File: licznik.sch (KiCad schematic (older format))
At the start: 23 parts, among them J1 Display, J2 Micro_SD_Card_Det, J3 Serial CS1, J4 Serial CS2, SW1 Wheel, SW2 Crank, SW3 Backlight, SW4 Right, SW5 Select, SW6 Left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

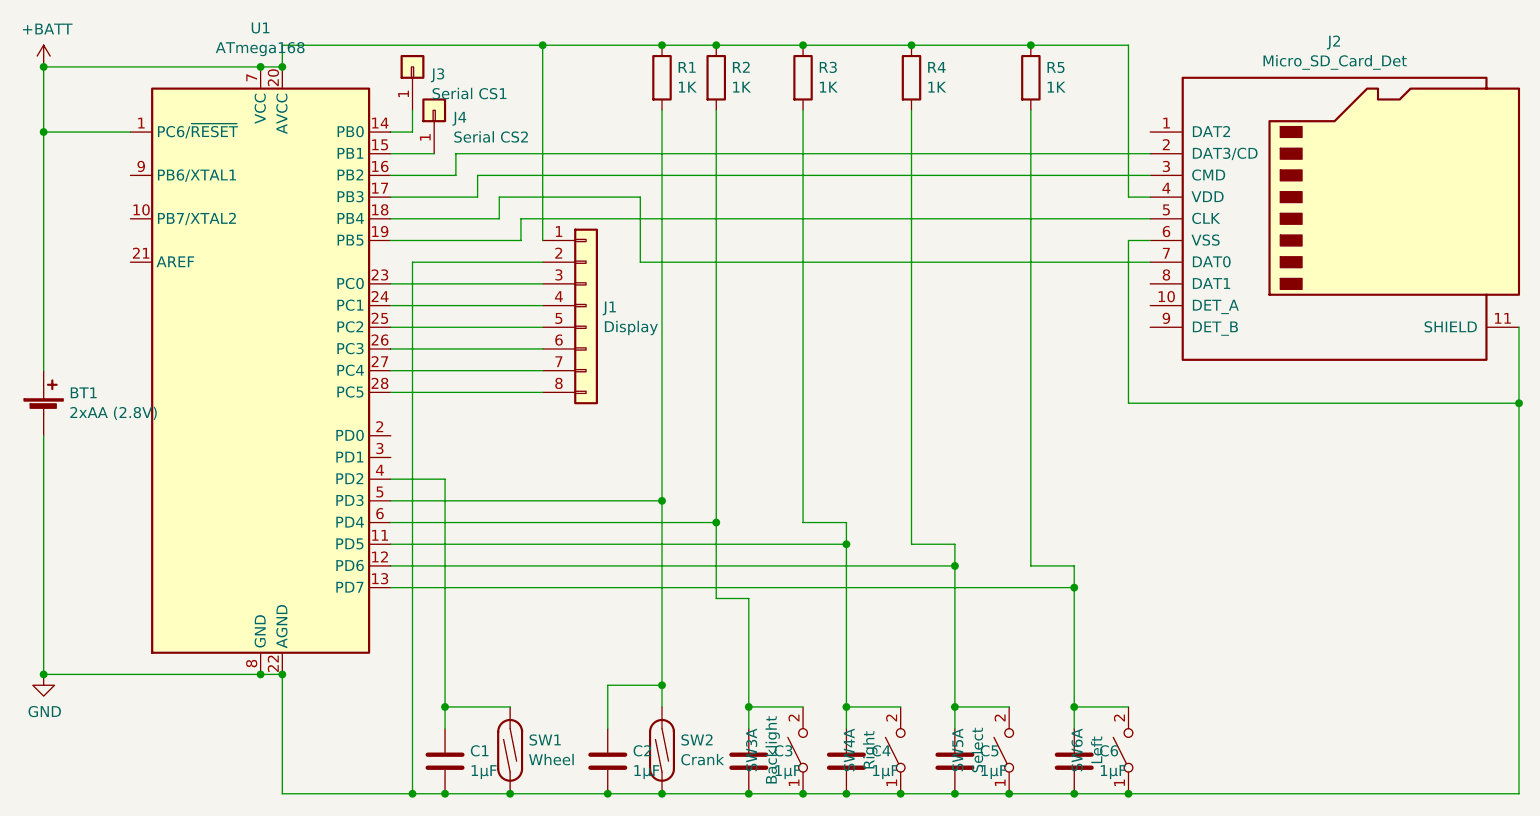
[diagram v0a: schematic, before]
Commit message: Add crank pull up resistor
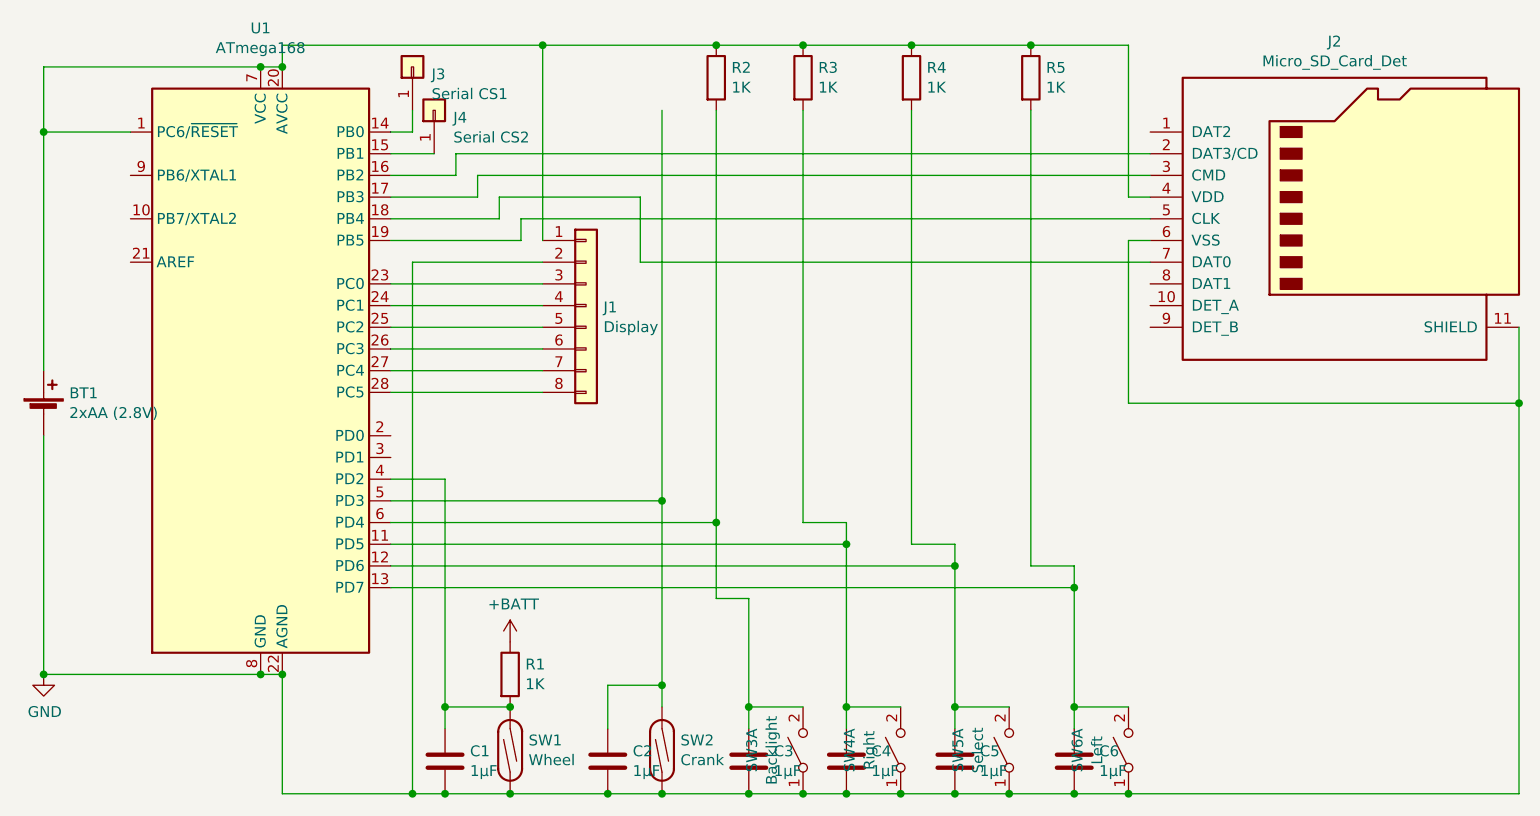
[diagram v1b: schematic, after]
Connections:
- net +BATT: no longer BT1.1 (+), J1.1 (Pin_1), J2.4 (VDD), R2.1, R3.1, R4.1, R5.1, U1.1 (PC6/~RESET), U1.20 (AVCC), U1.7 (VCC)
- net at C1.1, SW1.2, U1.4 (PD2): now also R1.2
- net at C2.1, SW2.2, U1.5 (PD3): no longer R1.2
- new net: BT1.1 (+), J1.1 (Pin_1), J2.4 (VDD), R2.1, R3.1, R4.1, R5.1, U1.1 (PC6/~RESET), U1.20 (AVCC), U1.7 (VCC)
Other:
- moved on the sheet: R1
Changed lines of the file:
@@
 L Device:R R1
 U 1 1 5BED8DEF
-P 5250 1050
-F 0 "R1" H 5320 1096 50  0000 L CNN
-F 1 "1K" H 5320 1005 50  0000 L CNN
-F 2 "Resistor_SMD:R_0603_1608Metric" V 5180 1050 50  0001 C CNN
-F 3 "~" H 5250 1050 50  0001 C CNN
-	1    5250 1050
+P 4550 3800
+F 0 "R1" H 4620 3846 50  0000 L CNN
+F 1 "1K" H 4620 3755 50  0000 L CNN
+F 2 "Resistor_SMD:R_0603_1608Metric" V 4480 3800 50  0001 C CNN
+F 3 "~" H 4550 3800 50  0001 C CNN
+	1    4550 3800
 	1    0    0    -1
 $EndComp
@@
 Wire Wire Line
 	4100 4350 4250 4350
-Connection ~ 5250 900
-Wire Wire Line
-	5250 900  5500 900
 Connection ~ 5500 900
 Wire Wire Line
@@
 Connection ~ 4700 900
 Wire Wire Line
-	4700 900  5250 900
-Wire Wire Line
 	4100 1900 4700 1900
 Wire Wire Line
@@
 L power:+BATT #PWR0102
 U 1 1 5BF4F9CB
-P 2400 1000
-F 0 "#PWR0102" H 2400 850 50  0001 C CNN
-F 1 "+BATT" H 2415 1173 50  0000 C CNN
-F 2 "" H 2400 1000 50  0001 C CNN
-F 3 "" H 2400 1000 50  0001 C CNN
-	1    2400 1000
-	1    0    0    -1
-$EndComp
-Connection ~ 2400 1000
+P 4550 3650
+F 0 "#PWR0102" H 4550 3500 50  0001 C CNN
+F 1 "+BATT" H 4565 3823 50  0000 C CNN
+F 2 "" H 4550 3650 50  0001 C CNN
+F 3 "" H 4550 3650 50  0001 C CNN
+	1    4550 3650
+	1    0    0    -1
+$EndComp
 $Comp
 L Connector_Generic:Conn_01x01 J3
@@
 Wire Wire Line
 	6100 4350 6350 4350
+Connection ~ 4550 3950
+Wire Wire Line
+	4700 900  5500 900
 $EndSCHEMATC

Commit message: Dimensions trim, reroute edy trace
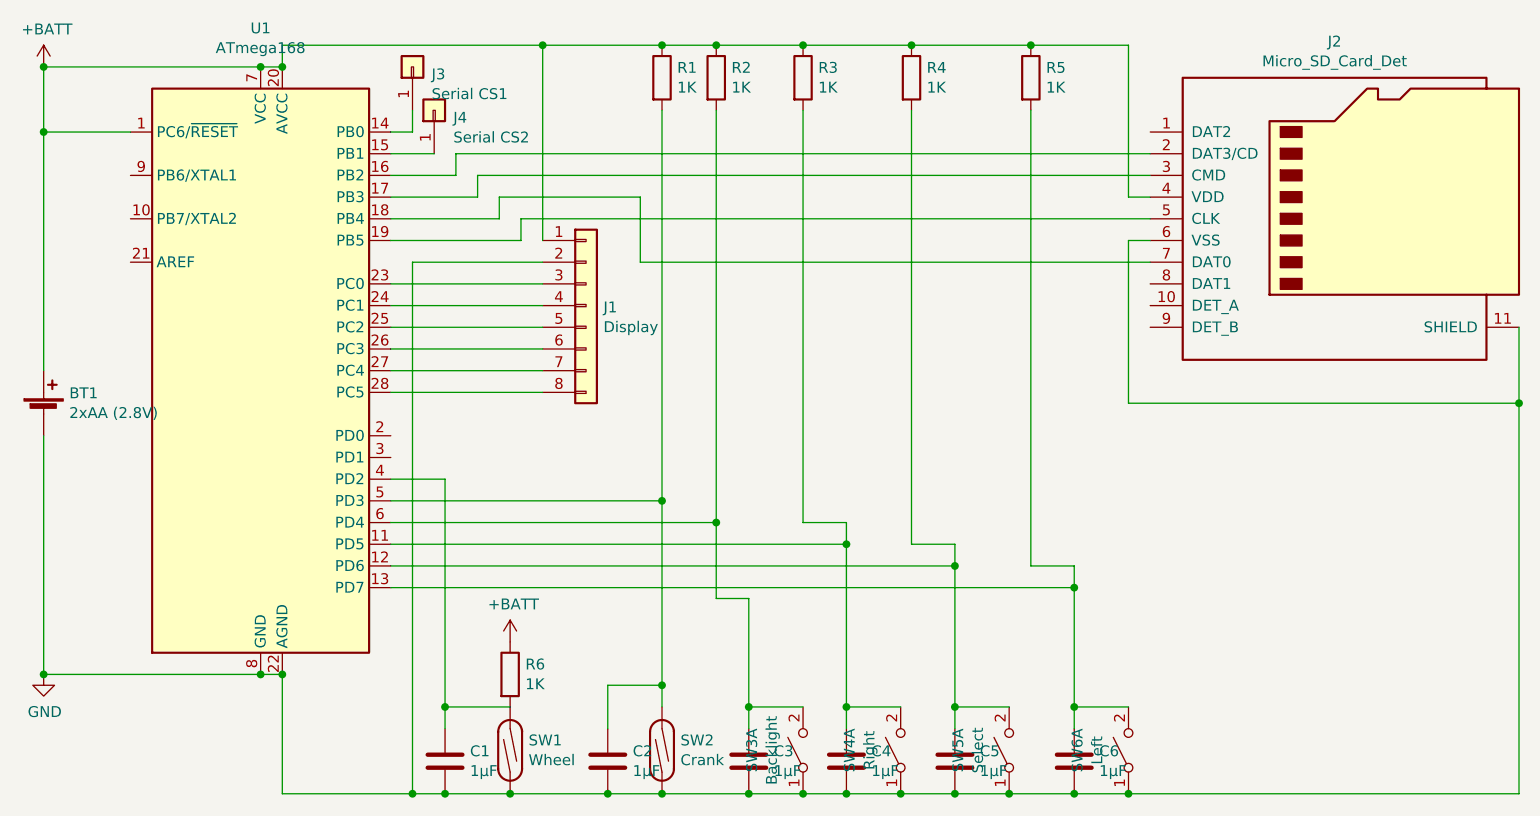
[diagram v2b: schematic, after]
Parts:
- added R6: 1K, Resistor_SMD:R_0603_1608Metric, symbol Device:R
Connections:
- net +BATT: now also BT1.1 (+), J1.1 (Pin_1), J2.4 (VDD), R2.1, R3.1, R4.1, R5.1, U1.1 (PC6/~RESET), U1.20 (AVCC), U1.7 (VCC), R6.1
- net at C1.1, SW1.2, U1.4 (PD2): now also R6.2; no longer R1.2
- net at C2.1, SW2.2, U1.5 (PD3): now also R1.2
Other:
- moved on the sheet: R1
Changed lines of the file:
@@
 L Device:R R1
 U 1 1 5BED8DEF
-P 4550 3800
-F 0 "R1" H 4620 3846 50  0000 L CNN
-F 1 "1K" H 4620 3755 50  0000 L CNN
-F 2 "Resistor_SMD:R_0603_1608Metric" V 4480 3800 50  0001 C CNN
-F 3 "~" H 4550 3800 50  0001 C CNN
-	1    4550 3800
+P 5250 1050
+F 0 "R1" H 5320 1096 50  0000 L CNN
+F 1 "1K" H 5320 1005 50  0000 L CNN
+F 2 "Resistor_SMD:R_0603_1608Metric" V 5180 1050 50  0001 C CNN
+F 3 "~" H 5250 1050 50  0001 C CNN
+	1    5250 1050
 	1    0    0    -1
 $EndComp
@@
 L power:+BATT #PWR0102
 U 1 1 5BF4F9CB
-P 4550 3650
-F 0 "#PWR0102" H 4550 3500 50  0001 C CNN
-F 1 "+BATT" H 4565 3823 50  0000 C CNN
-F 2 "" H 4550 3650 50  0001 C CNN
-F 3 "" H 4550 3650 50  0001 C CNN
-	1    4550 3650
+P 2400 1000
+F 0 "#PWR0102" H 2400 850 50  0001 C CNN
+F 1 "+BATT" H 2415 1173 50  0000 C CNN
+F 2 "" H 2400 1000 50  0001 C CNN
+F 3 "" H 2400 1000 50  0001 C CNN
+	1    2400 1000
 	1    0    0    -1
 $EndComp
@@
 Wire Wire Line
 	6100 4350 6350 4350
-Connection ~ 4550 3950
-Wire Wire Line
-	4700 900  5500 900
+Wire Wire Line
+	4700 900  5250 900
+Wire Wire Line
+	5250 900  5500 900
+Connection ~ 5250 900
+Connection ~ 2400 1000
+$Comp
+L Device:R R6
+U 1 1 5BF3E7C4
+P 4550 3800
+F 0 "R6" H 4620 3846 50  0000 L CNN
+F 1 "1K" H 4620 3755 50  0000 L CNN
+F 2 "Resistor_SMD:R_0603_1608Metric" V 4480 3800 50  0001 C CNN
+F 3 "~" H 4550 3800 50  0001 C CNN
+	1    4550 3800
+	1    0    0    -1
+$EndComp
+$Comp
+L power:+BATT #PWR0103
+U 1 1 5BF418F0
+P 4550 3650
+F 0 "#PWR0103" H 4550 3500 50  0001 C CNN
+F 1 "+BATT" H 4565 3823 50  0000 C CNN
+F 2 "" H 4550 3650 50  0001 C CNN
+F 3 "" H 4550 3650 50  0001 C CNN
+	1    4550 3650
+	1    0    0    -1
+$EndComp
 $EndSCHEMATC
